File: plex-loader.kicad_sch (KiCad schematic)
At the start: 23 parts, among them J1 Conn_01x05_Pin, J10 Conn_02x05_Odd_Even, J2 Conn_01x05_Pin, J3 Conn_01x05_Pin, J4 Conn_01x05_Pin, J5 Conn_01x05_Pin, J9 Conn_02x20_Odd_Even, U1 TMUX1208PWR, U2 TMUX1208PWR, U3 TMUX1208PWR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

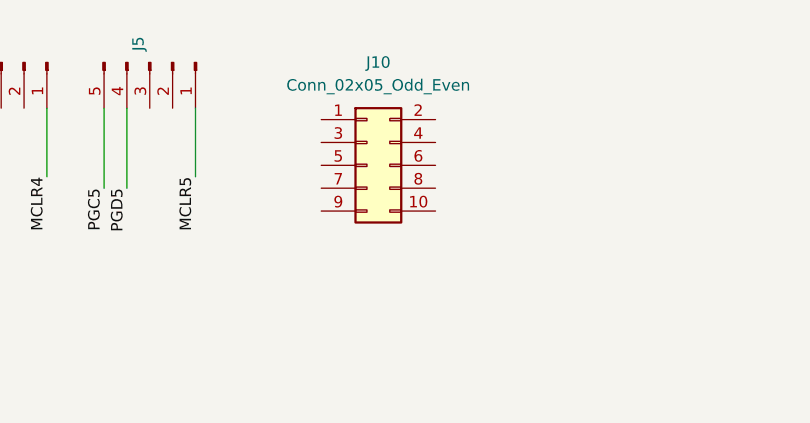
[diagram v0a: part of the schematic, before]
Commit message: switched footprint
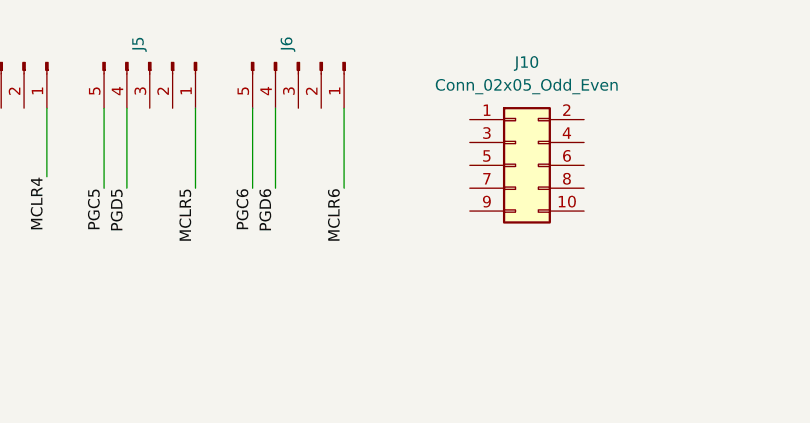
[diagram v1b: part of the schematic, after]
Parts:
- added J6: Conn_01x05_Pin, Connector_Hirose:Hirose_DF13-05P-1.25DS_1x05_P1.25mm_Horizontal, symbol Connector:Conn_01x05_Pin
- J1, J2, J3, J4, J5: footprint Connector_JST:JST_GH_SM05B-GHS-TB_1x05-1MP_P1.25mm_Horizontal -> Connector_Hirose:Hirose_DF13-05P-1.25DS_1x05_P1.25mm_Horizontal
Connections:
- net MCLR6: now also J6.1 (Pin_1)
- net PGC6: now also J6.5 (Pin_5)
- net PGD6: now also J6.4 (Pin_4)
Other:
- moved on the sheet: J10
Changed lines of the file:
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@@
 	(wire
 		(pts
+			(xy 107.95 30.48) (xy 107.95 39.37)
+		)
+		(stroke
+			(width 0)
+			(type default)
+		)
+	)
+	(wire
+		(pts
 			(xy 220.98 104.14) (xy 195.58 104.14)
 		)
@@
 	(wire
 		(pts
+			(xy 118.11 30.48) (xy 118.11 39.37)
+		)
+		(stroke
+			(width 0)
+			(type default)
+		)
+	)
+	(wire
+		(pts
 			(xy 146.05 166.37) (xy 146.05 161.29)
 		)
@@
 	(wire
 		(pts
-			(xy 101.6 30.48) (xy 101.6 38.1)
+			(xy 101.6 30.48) (xy 101.6 39.37)
 		)
 		(stroke
@@
 	(wire
 		(pts
+			(xy 110.49 30.48) (xy 110.49 39.37)
+		)
+		(stroke
+			(width 0)
+			(type default)
+		)
+	)
+	(wire
+		(pts
 			(xy 269.24 144.78) (xy 261.62 144.78)
 		)
@@
 		)
 	)
+	(label "PGD6"
+		(at 110.49 39.37 270)
+		(fields_autoplaced yes)
+		(effects
+			(font
+				(size 1.27 1.27)
+			)
+			(justify right bottom)
+		)
+	)
+	(label "MCLR6"
+		(at 118.11 39.37 270)
+		(fields_autoplaced yes)
+		(effects
+			(font
+				(size 1.27 1.27)
+			)
+			(justify right bottom)
+		)
+	)
 	(label "GPIO27"
 		(at 210.82 71.12 180)
@@
 	)
 	(label "MCLR5"
-		(at 101.6 38.1 270)
+		(at 101.6 39.37 270)
 		(fields_autoplaced yes)
 		(effects
@@
 		)
 	)
+	(label "PGC6"
+		(at 107.95 39.37 270)
+		(fields_autoplaced yes)
+		(effects
+			(font
+				(size 1.27 1.27)
+			)
+			(justify right bottom)
+		)
+	)
 	(label "GPIO10"
 		(at 270.51 68.58 0)
@@
 			)
 		)
-		(property "Footprint" "Connector_JST:JST_GH_SM05B-GHS-TB_1x05-1MP_P1.25mm_Horizontal"
+		(property "Footprint" "Connector_Hirose:Hirose_DF13-05P-1.25DS_1x05_P1.25mm_Horizontal"
 			(at 96.52 25.4 0)
 			(effects
@@
 	(symbol
 		(lib_id "Connector_Generic:Conn_02x05_Odd_Even")
-		(at 120.65 36.83 0)
+		(at 137.16 36.83 0)
 		(unit 1)
 		(exclude_from_sim no)
@@
 		(fields_autoplaced yes)
 		(property "Reference" "J10"
-			(at 121.92 25.4 0)
+			(at 138.43 25.4 0)
 			(effects
 				(font
@@
 		)
 		(property "Value" "Conn_02x05_Odd_Even"
-			(at 121.92 27.94 0)
+			(at 138.43 27.94 0)
 			(effects
 				(font
@@
 		)
 		(property "Footprint" "Connector_PinHeader_2.54mm:PinHeader_2x05_P2.54mm_Vertical"
-			(at 120.65 36.83 0)
+			(at 137.16 36.83 0)
 			(effects
 				(font
@@
 		)
 		(property "Datasheet" "~"
-			(at 120.65 36.83 0)
+			(at 137.16 36.83 0)
 			(effects
 				(font
@@
 		)
 		(property "Description" "Generic connector, double row, 02x05, odd/even pin numbering scheme (row 1 odd numbers, row 2 even numbers), script generated (kicad-library-utils/schlib/autogen/connector/)"
-			(at 120.65 36.83 0)
+			(at 137.16 36.83 0)
 			(effects
 				(font
@@
 			)
 		)
-		(property "Footprint" "Connector_JST:JST_GH_SM05B-GHS-TB_1x05-1MP_P1.25mm_Horizontal"
+		(property "Footprint" "Connector_Hirose:Hirose_DF13-05P-1.25DS_1x05_P1.25mm_Horizontal"
 			(at 80.01 25.4 0)
 			(effects
@@
 	(symbol
 		(lib_id "Connector:Conn_01x05_Pin")
+		(at 113.03 25.4 270)
+		(unit 1)
+		(exclude_from_sim no)
+		(in_bom yes)
+		(on_board yes)
+		(dnp no)
+		(fields_autoplaced yes)
+		(property "Reference" "J6"
+			(at 111.7599 24.13 0)
+			(effects
+				(font
+					(size 1.27 1.27)
+				)
+				(justify right)
+			)
+		)
+		(property "Value" "Conn_01x05_Pin"
+			(at 114.2999 24.13 0)
+			(effects
+				(font
+					(size 1.27 1.27)
+				)
+				(justify right)
+				(hide yes)
+			)
+		)
+		(property "Footprint" "Connector_Hirose:Hirose_DF13-05P-1.25DS_1x05_P1.25mm_Horizontal"
+			(at 113.03 25.4 0)
+			(effects
+				(font
+					(size 1.27 1.27)
+				)
+				(hide yes)
+			)
+		)
+		(property "Datasheet" "~"
+			(at 113.03 25.4 0)
+			(effects
+				(font
+					(size 1.27 1.27)
+				)
+				(hide yes)
+			)
+		)
+		(property "Description" "Generic connector, single row, 01x05, script generated"
+			(at 113.03 25.4 0)
+			(effects
+				(font
+					(size 1.27 1.27)
+				)
+				(hide yes)
+			)
+		)
+		(pin "5"
+		)
+		(pin "4"
+		)
+		(pin "1"
+		)
+		(pin "2"
+		)
+		(pin "3"
+		)
+		(instances
+			(project "plex-loader"
+				(path "/347fd5f2-11b0-457c-a5f0-e6d947a3628e"
+					(reference "J6")
+					(unit 1)
+				)
+			)
+		)
+	)
+	(symbol
+		(lib_id "Connector:Conn_01x05_Pin")
 		(at 46.99 25.4 270)
 		(unit 1)
@@
 			)
 		)
-		(property "Footprint" "Connector_JST:JST_GH_SM05B-GHS-TB_1x05-1MP_P1.25mm_Horizontal"
+		(property "Footprint" "Connector_Hirose:Hirose_DF13-05P-1.25DS_1x05_P1.25mm_Horizontal"
 			(at 46.99 25.4 0)
 			(effects
@@
 			)
 		)
-		(property "Footprint" "Connector_JST:JST_GH_SM05B-GHS-TB_1x05-1MP_P1.25mm_Horizontal"
+		(property "Footprint" "Connector_Hirose:Hirose_DF13-05P-1.25DS_1x05_P1.25mm_Horizontal"
 			(at 30.48 25.4 0)
 			(effects
@@
 			)
 		)
-		(property "Footprint" "Connector_JST:JST_GH_SM05B-GHS-TB_1x05-1MP_P1.25mm_Horizontal"
+		(property "Footprint" "Connector_Hirose:Hirose_DF13-05P-1.25DS_1x05_P1.25mm_Horizontal"
 			(at 63.5 25.4 0)
 			(effects

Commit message: update layers
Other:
- moved on the sheet: R10
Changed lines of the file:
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@@
 	(wire
 		(pts
-			(xy 264.16 35.56) (xy 264.16 39.37)
+			(xy 261.62 35.56) (xy 261.62 39.37)
 		)
 		(stroke
@@
 	(wire
 		(pts
-			(xy 264.16 22.86) (xy 264.16 27.94)
+			(xy 261.62 22.86) (xy 261.62 27.94)
 		)
 		(stroke
@@
 	)
 	(label "GPIO10"
-		(at 264.16 22.86 180)
+		(at 261.62 22.86 180)
 		(fields_autoplaced yes)
 		(effects
@@
 	(symbol
 		(lib_id "Device:R")
-		(at 264.16 31.75 0)
+		(at 261.62 31.75 0)
 		(unit 1)
 		(exclude_from_sim no)
@@
 		(dnp no)
 		(property "Reference" "R10"
-			(at 266.192 32.512 0)
+			(at 263.652 32.512 0)
 			(effects
 				(font
@@
 		)
 		(property "Value" "10k"
-			(at 266.192 29.972 0)
+			(at 263.652 29.972 0)
 			(effects
 				(font
@@
 		)
 		(property "Footprint" "Resistor_SMD:R_0603_1608Metric"
-			(at 262.382 31.75 90)
+			(at 259.842 31.75 90)
 			(effects
 				(font
@@
 		)
 		(property "Datasheet" "~"
-			(at 264.16 31.75 0)
+			(at 261.62 31.75 0)
 			(effects
 				(font
@@
 		)
 		(property "Description" "Resistor"
-			(at 264.16 31.75 0)
+			(at 261.62 31.75 0)
 			(effects
 				(font
@@
 	(symbol
 		(lib_id "power:GND")
-		(at 264.16 39.37 0)
+		(at 261.62 39.37 0)
 		(unit 1)
 		(exclude_from_sim no)
@@
 		(dnp no)
 		(property "Reference" "#PWR05"
-			(at 264.16 45.72 0)
+			(at 261.62 45.72 0)
 			(effects
 				(font
@@
 		)
 		(property "Value" "GND"
-			(at 264.16 44.45 0)
+			(at 261.62 44.45 0)
 			(effects
 				(font
@@
 		)
 		(property "Footprint" ""
-			(at 264.16 39.37 0)
+			(at 261.62 39.37 0)
 			(effects
 				(font
@@
 		)
 		(property "Datasheet" ""
-			(at 264.16 39.37 0)
+			(at 261.62 39.37 0)
 			(effects
 				(font
@@
 		)
 		(property "Description" "Power symbol creates a global label with name \"GND\" , ground"
-			(at 264.16 39.37 0)
-			(effects
-				(font
+			(at 261.62 39.37 0)
+			(effects
+				(font

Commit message: route draft
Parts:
- D1: footprint LED_SMD:LED_0603_1608Metric -> LED_SMD:LED_0805_2012Metric
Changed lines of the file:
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@@
 		)
 	)
-	(label "PDG8"
+	(label "PGD8"
 		(at 97.79 170.18 180)
 		(fields_autoplaced yes)
@@
 			)
 		)
-		(property "Footprint" "LED_SMD:LED_0603_1608Metric"
+		(property "Footprint" "LED_SMD:LED_0805_2012Metric"
 			(at 74.93 172.72 0)
 			(effects
